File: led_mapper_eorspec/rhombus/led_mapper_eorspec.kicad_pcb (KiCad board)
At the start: 4 copper layers, 116 x 67 mm, 513 parts, among them J1 Conn_02x12_Top_Bottom

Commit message: sync PCB changes
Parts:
- moved J1 151.1 mm to (103.6, 41.4)
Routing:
- net /P6: track 91.7 -> 129.4 mm
- net /P1: track 96.8 -> 132.7 mm
- net /P2: track 94.7 -> 130.3 mm
- net /P3: track 94.7 -> 130.0 mm
- net /P4: track 94.7 -> 129.7 mm
- net /P5: track 94.7 -> 129.4 mm
- net /P7: track 94.7 -> 128.8 mm
- net /P8: track 96.8 -> 130.6 mm
- net /P23: track 100.0 -> 97.0 mm
- net /P19: track 114.7 -> 111.7 mm
- net /P16: track 114.7 -> 111.7 mm
- net /P13: track 114.7 -> 111.7 mm
- net /P10: track 114.7 -> 111.7 mm
- net /P22: track 100.0 -> 97.0 mm
- net /P20: track 100.0 -> 97.0 mm
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
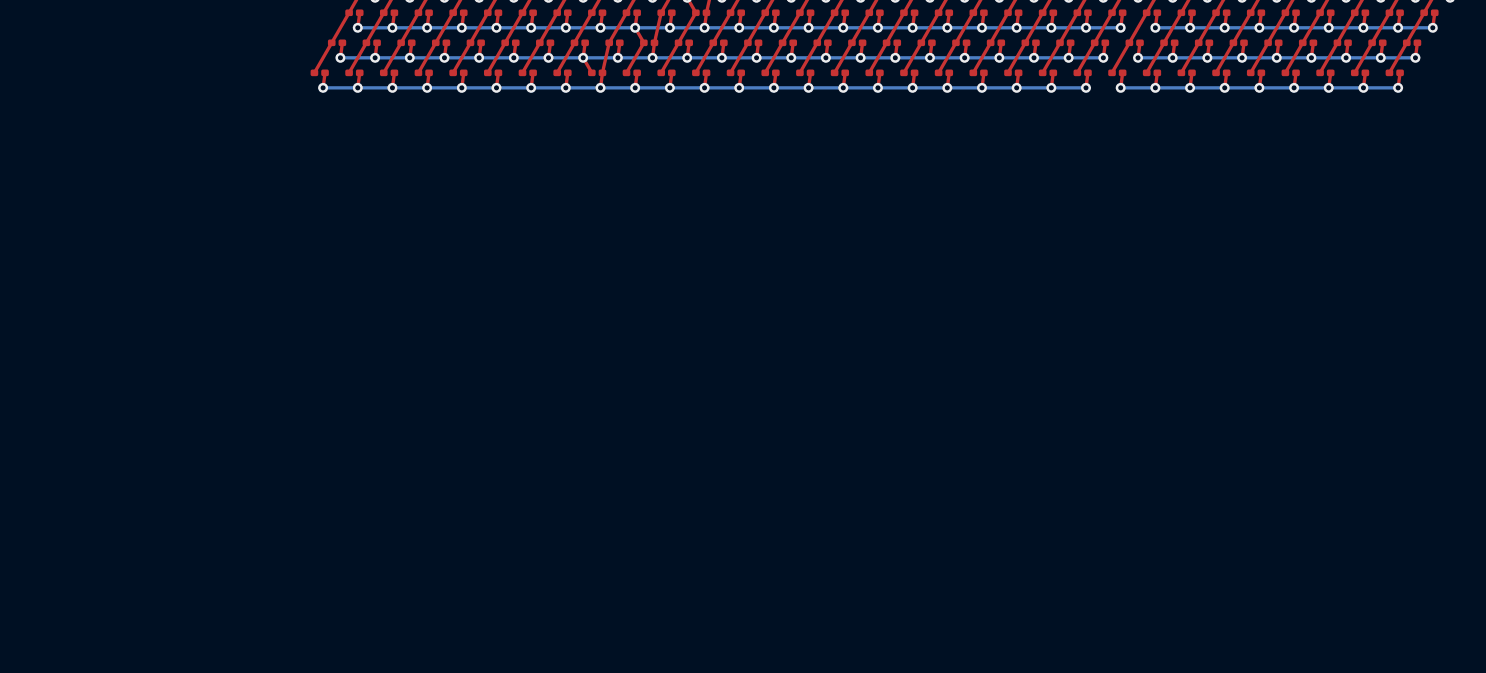
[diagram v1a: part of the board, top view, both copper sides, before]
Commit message: Add second network to PCB
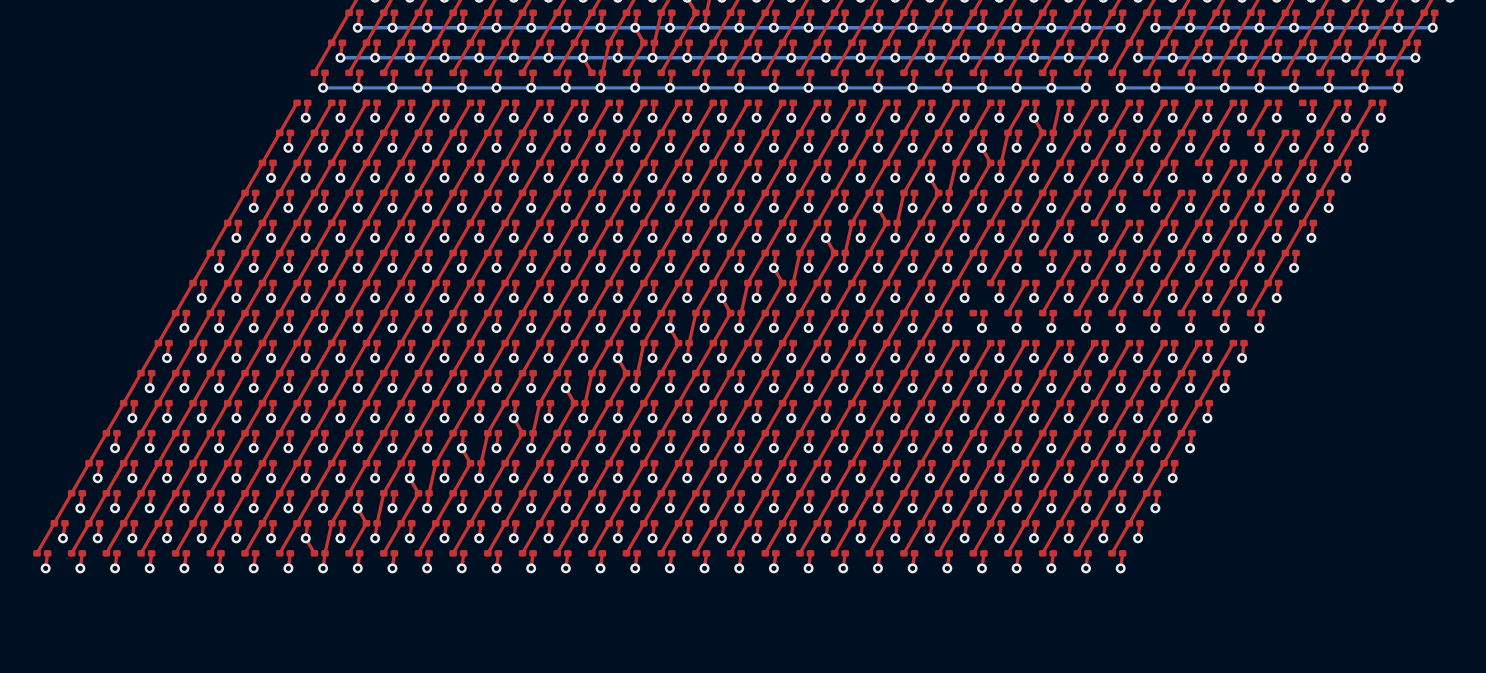
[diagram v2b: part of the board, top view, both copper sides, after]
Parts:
- added D1000: LED_45deg, LED_SMD:LED_0201_0603Metric, F.Cu at (13.9, 75.0)
- added D1001: LED_45deg, LED_SMD:LED_0201_0603Metric, F.Cu at (16.0, 75.0)
- added D1002: LED_45deg, LED_SMD:LED_0201_0603Metric, F.Cu at (18.1, 75.0)
- added D1003: LED_45deg, LED_SMD:LED_0201_0603Metric, F.Cu at (20.2, 75.0)
- added D1004: LED_45deg, LED_SMD:LED_0201_0603Metric, F.Cu at (22.3, 75.0)
- added D1005: LED_45deg, LED_SMD:LED_0201_0603Metric, F.Cu at (24.4, 75.0)
- added D1006: LED_45deg, LED_SMD:LED_0201_0603Metric, F.Cu at (26.4, 75.0)
- added D1007: LED_45deg, LED_SMD:LED_0201_0603Metric, F.Cu at (28.5, 75.0)
- added D1008: LED_45deg, LED_SMD:LED_0201_0603Metric, F.Cu at (30.6, 75.0)
- added D1009: LED_45deg, LED_SMD:LED_0201_0603Metric, F.Cu at (32.7, 75.0)
- added D1010: LED_45deg, LED_SMD:LED_0201_0603Metric, F.Cu at (34.8, 75.0)
- added D1011: LED_45deg, LED_SMD:LED_0201_0603Metric, F.Cu at (36.9, 75.0)
- added D1012: LED_45deg, LED_SMD:LED_0201_0603Metric, F.Cu at (39.0, 75.0)
- added D1013: LED_45deg, LED_SMD:LED_0201_0603Metric, F.Cu at (41.1, 75.0)
- added D1014: LED_45deg, LED_SMD:LED_0201_0603Metric, F.Cu at (43.2, 75.0)
- added D1015: LED_45deg, LED_SMD:LED_0201_0603Metric, F.Cu at (45.3, 75.0)
- added D1016: LED_45deg, LED_SMD:LED_0201_0603Metric, F.Cu at (47.4, 75.0)
- added D1017: LED_45deg, LED_SMD:LED_0201_0603Metric, F.Cu at (49.4, 75.0)
- added D1018: LED_45deg, LED_SMD:LED_0201_0603Metric, F.Cu at (51.5, 75.0)
- added D1019: LED_45deg, LED_SMD:LED_0201_0603Metric, F.Cu at (53.6, 75.0)
- added D1020: LED_45deg, LED_SMD:LED_0201_0603Metric, F.Cu at (55.7, 75.0)
- added D1021: LED_45deg, LED_SMD:LED_0201_0603Metric, F.Cu at (57.8, 75.0)
- added D1022: LED_45deg, LED_SMD:LED_0201_0603Metric, F.Cu at (59.9, 75.0)
- added D1023: LED_45deg, LED_SMD:LED_0201_0603Metric, F.Cu at (62.0, 75.0)
- added D1024: LED_45deg, LED_SMD:LED_0201_0603Metric, F.Cu at (64.1, 75.0)
- added D513: LED_45deg, LED_SMD:LED_0201_0603Metric, F.Cu at (15.0, 47.8)
- added D514: LED_45deg, LED_SMD:LED_0201_0603Metric, F.Cu at (17.0, 47.8)
- added D515: LED_45deg, LED_SMD:LED_0201_0603Metric, F.Cu at (19.1, 47.8)
- added D516: LED_45deg, LED_SMD:LED_0201_0603Metric, F.Cu at (21.2, 47.8)
- added D517: LED_45deg, LED_SMD:LED_0201_0603Metric, F.Cu at (23.3, 47.8)
- added D518: LED_45deg, LED_SMD:LED_0201_0603Metric, F.Cu at (25.4, 47.8)
- added D519: LED_45deg, LED_SMD:LED_0201_0603Metric, F.Cu at (27.5, 47.8)
- added D520: LED_45deg, LED_SMD:LED_0201_0603Metric, F.Cu at (29.6, 47.8)
- added D521: LED_45deg, LED_SMD:LED_0201_0603Metric, F.Cu at (31.7, 47.8)
- added D522: LED_45deg, LED_SMD:LED_0201_0603Metric, F.Cu at (33.8, 47.8)
- added D523: LED_45deg, LED_SMD:LED_0201_0603Metric, F.Cu at (35.9, 47.8)
- added D524: LED_45deg, LED_SMD:LED_0201_0603Metric, F.Cu at (37.9, 47.8)
- added D525: LED_45deg, LED_SMD:LED_0201_0603Metric, F.Cu at (40.0, 47.8)
- added D526: LED_45deg, LED_SMD:LED_0201_0603Metric, F.Cu at (42.1, 47.8)
- added D527: LED_45deg, LED_SMD:LED_0201_0603Metric, F.Cu at (44.2, 47.8)
- added D528: LED_45deg, LED_SMD:LED_0201_0603Metric, F.Cu at (46.3, 47.8)
- added D529: LED_45deg, LED_SMD:LED_0201_0603Metric, F.Cu at (48.4, 47.8)
- added D530: LED_45deg, LED_SMD:LED_0201_0603Metric, F.Cu at (50.5, 47.8)
- added D531: LED_45deg, LED_SMD:LED_0201_0603Metric, F.Cu at (52.6, 47.8)
- added D532: LED_45deg, LED_SMD:LED_0201_0603Metric, F.Cu at (54.7, 47.8)
- added D533: LED_45deg, LED_SMD:LED_0201_0603Metric, F.Cu at (56.8, 47.8)
- added D534: LED_45deg, LED_SMD:LED_0201_0603Metric, F.Cu at (58.8, 47.8)
- added D535: LED_45deg, LED_SMD:LED_0201_0603Metric, F.Cu at (60.9, 47.8)
- added D536: LED_45deg, LED_SMD:LED_0201_0603Metric, F.Cu at (63.0, 47.8)
- added D537: LED_45deg, LED_SMD:LED_0201_0603Metric, F.Cu at (65.1, 47.8)
- added D538: LED_45deg, LED_SMD:LED_0201_0603Metric, F.Cu at (67.2, 47.8)
- added D539: LED_45deg, LED_SMD:LED_0201_0603Metric, F.Cu at (69.3, 47.8)
- added D540: LED_45deg, LED_SMD:LED_0201_0603Metric, F.Cu at (71.4, 47.8)
- added D541: LED_45deg, LED_SMD:LED_0201_0603Metric, F.Cu at (73.5, 47.8)
- added D542: LED_45deg, LED_SMD:LED_0201_0603Metric, F.Cu at (75.6, 47.8)
- added D543: LED_45deg, LED_SMD:LED_0201_0603Metric, F.Cu at (77.7, 47.8)
- added D544: LED_45deg, LED_SMD:LED_0201_0603Metric, F.Cu at (79.7, 47.8)
- added D545: LED_45deg, LED_SMD:LED_0201_0603Metric, F.Cu at (13.9, 49.6)
- added D546: LED_45deg, LED_SMD:LED_0201_0603Metric, F.Cu at (16.0, 49.6)
- added D547: LED_45deg, LED_SMD:LED_0201_0603Metric, F.Cu at (18.1, 49.6)
- added D548: LED_45deg, LED_SMD:LED_0201_0603Metric, F.Cu at (20.2, 49.6)
- added D549: LED_45deg, LED_SMD:LED_0201_0603Metric, F.Cu at (22.3, 49.6)
- added D550: LED_45deg, LED_SMD:LED_0201_0603Metric, F.Cu at (24.4, 49.6)
- added D551: LED_45deg, LED_SMD:LED_0201_0603Metric, F.Cu at (26.4, 49.6)
- added D552: LED_45deg, LED_SMD:LED_0201_0603Metric, F.Cu at (28.5, 49.6)
- added D553: LED_45deg, LED_SMD:LED_0201_0603Metric, F.Cu at (30.6, 49.6)
- added D554: LED_45deg, LED_SMD:LED_0201_0603Metric, F.Cu at (32.7, 49.6)
- added D555: LED_45deg, LED_SMD:LED_0201_0603Metric, F.Cu at (34.8, 49.6)
- added D556: LED_45deg, LED_SMD:LED_0201_0603Metric, F.Cu at (36.9, 49.6)
- added D557: LED_45deg, LED_SMD:LED_0201_0603Metric, F.Cu at (39.0, 49.6)
- added D558: LED_45deg, LED_SMD:LED_0201_0603Metric, F.Cu at (41.1, 49.6)
- added D559: LED_45deg, LED_SMD:LED_0201_0603Metric, F.Cu at (43.2, 49.6)
- added D560: LED_45deg, LED_SMD:LED_0201_0603Metric, F.Cu at (45.3, 49.6)
- added D561: LED_45deg, LED_SMD:LED_0201_0603Metric, F.Cu at (47.4, 49.6)
- added D562: LED_45deg, LED_SMD:LED_0201_0603Metric, F.Cu at (49.4, 49.6)
- added D563: LED_45deg, LED_SMD:LED_0201_0603Metric, F.Cu at (51.5, 49.6)
- added D564: LED_45deg, LED_SMD:LED_0201_0603Metric, F.Cu at (53.6, 49.6)
- added D565: LED_45deg, LED_SMD:LED_0201_0603Metric, F.Cu at (55.7, 49.6)
- added D566: LED_45deg, LED_SMD:LED_0201_0603Metric, F.Cu at (57.8, 49.6)
- added D567: LED_45deg, LED_SMD:LED_0201_0603Metric, F.Cu at (59.9, 49.6)
- added D568: LED_45deg, LED_SMD:LED_0201_0603Metric, F.Cu at (62.0, 49.6)
- added D569: LED_45deg, LED_SMD:LED_0201_0603Metric, F.Cu at (64.1, 49.6)
- added D570: LED_45deg, LED_SMD:LED_0201_0603Metric, F.Cu at (66.2, 49.6)
- added D571: LED_45deg, LED_SMD:LED_0201_0603Metric, F.Cu at (68.2, 49.6)
- added D572: LED_45deg, LED_SMD:LED_0201_0603Metric, F.Cu at (70.3, 49.6)
- added D573: LED_45deg, LED_SMD:LED_0201_0603Metric, F.Cu at (72.4, 49.6)
- added D574: LED_45deg, LED_SMD:LED_0201_0603Metric, F.Cu at (74.5, 49.6)
- added D575: LED_45deg, LED_SMD:LED_0201_0603Metric, F.Cu at (76.6, 49.6)
- added D576: LED_45deg, LED_SMD:LED_0201_0603Metric, F.Cu at (78.7, 49.6)
- added D577: LED_45deg, LED_SMD:LED_0201_0603Metric, F.Cu at (12.9, 51.4)
- added D578: LED_45deg, LED_SMD:LED_0201_0603Metric, F.Cu at (15.0, 51.4)
- added D579: LED_45deg, LED_SMD:LED_0201_0603Metric, F.Cu at (17.0, 51.4)
- added D580: LED_45deg, LED_SMD:LED_0201_0603Metric, F.Cu at (19.1, 51.4)
- added D581: LED_45deg, LED_SMD:LED_0201_0603Metric, F.Cu at (21.2, 51.4)
- added D582: LED_45deg, LED_SMD:LED_0201_0603Metric, F.Cu at (23.3, 51.4)
- added D583: LED_45deg, LED_SMD:LED_0201_0603Metric, F.Cu at (25.4, 51.4)
- added D584: LED_45deg, LED_SMD:LED_0201_0603Metric, F.Cu at (27.5, 51.4)
- added D585: LED_45deg, LED_SMD:LED_0201_0603Metric, F.Cu at (29.6, 51.4)
- added D586: LED_45deg, LED_SMD:LED_0201_0603Metric, F.Cu at (31.7, 51.4)
- added D587: LED_45deg, LED_SMD:LED_0201_0603Metric, F.Cu at (33.8, 51.4)
- added D588: LED_45deg, LED_SMD:LED_0201_0603Metric, F.Cu at (35.9, 51.4)
- added D589: LED_45deg, LED_SMD:LED_0201_0603Metric, F.Cu at (37.9, 51.4)
- added D590: LED_45deg, LED_SMD:LED_0201_0603Metric, F.Cu at (40.0, 51.4)
- added D591: LED_45deg, LED_SMD:LED_0201_0603Metric, F.Cu at (42.1, 51.4)
- added D592: LED_45deg, LED_SMD:LED_0201_0603Metric, F.Cu at (44.2, 51.4)
- added D593: LED_45deg, LED_SMD:LED_0201_0603Metric, F.Cu at (46.3, 51.4)
- added D594: LED_45deg, LED_SMD:LED_0201_0603Metric, F.Cu at (48.4, 51.4)
- added D595: LED_45deg, LED_SMD:LED_0201_0603Metric, F.Cu at (50.5, 51.4)
- added D596: LED_45deg, LED_SMD:LED_0201_0603Metric, F.Cu at (52.6, 51.4)
- added D597: LED_45deg, LED_SMD:LED_0201_0603Metric, F.Cu at (54.7, 51.4)
- added D598: LED_45deg, LED_SMD:LED_0201_0603Metric, F.Cu at (56.8, 51.4)
- added D599: LED_45deg, LED_SMD:LED_0201_0603Metric, F.Cu at (58.8, 51.4)
- added D600: LED_45deg, LED_SMD:LED_0201_0603Metric, F.Cu at (60.9, 51.4)
- added D601: LED_45deg, LED_SMD:LED_0201_0603Metric, F.Cu at (63.0, 51.4)
- added D602: LED_45deg, LED_SMD:LED_0201_0603Metric, F.Cu at (65.1, 51.4)
- added D603: LED_45deg, LED_SMD:LED_0201_0603Metric, F.Cu at (67.2, 51.4)
- added D604: LED_45deg, LED_SMD:LED_0201_0603Metric, F.Cu at (69.3, 51.4)
- added D605: LED_45deg, LED_SMD:LED_0201_0603Metric, F.Cu at (71.4, 51.4)
- added D606: LED_45deg, LED_SMD:LED_0201_0603Metric, F.Cu at (73.5, 51.4)
- added D607: LED_45deg, LED_SMD:LED_0201_0603Metric, F.Cu at (75.6, 51.4)
- added D608: LED_45deg, LED_SMD:LED_0201_0603Metric, F.Cu at (77.7, 51.4)
- added D609: LED_45deg, LED_SMD:LED_0201_0603Metric, F.Cu at (11.8, 53.2)
- added D610: LED_45deg, LED_SMD:LED_0201_0603Metric, F.Cu at (13.9, 53.2)
- added D611: LED_45deg, LED_SMD:LED_0201_0603Metric, F.Cu at (16.0, 53.2)
- added D612: LED_45deg, LED_SMD:LED_0201_0603Metric, F.Cu at (18.1, 53.2)
- added D613: LED_45deg, LED_SMD:LED_0201_0603Metric, F.Cu at (20.2, 53.2)
- added D614: LED_45deg, LED_SMD:LED_0201_0603Metric, F.Cu at (22.3, 53.2)
- added D615: LED_45deg, LED_SMD:LED_0201_0603Metric, F.Cu at (24.4, 53.2)
- added D616: LED_45deg, LED_SMD:LED_0201_0603Metric, F.Cu at (26.4, 53.2)
- added D617: LED_45deg, LED_SMD:LED_0201_0603Metric, F.Cu at (28.5, 53.2)
- added D618: LED_45deg, LED_SMD:LED_0201_0603Metric, F.Cu at (30.6, 53.2)
- added D619: LED_45deg, LED_SMD:LED_0201_0603Metric, F.Cu at (32.7, 53.2)
- added D620: LED_45deg, LED_SMD:LED_0201_0603Metric, F.Cu at (34.8, 53.2)
- added D621: LED_45deg, LED_SMD:LED_0201_0603Metric, F.Cu at (36.9, 53.2)
- added D622: LED_45deg, LED_SMD:LED_0201_0603Metric, F.Cu at (39.0, 53.2)
- added D623: LED_45deg, LED_SMD:LED_0201_0603Metric, F.Cu at (41.1, 53.2)
- added D624: LED_45deg, LED_SMD:LED_0201_0603Metric, F.Cu at (43.2, 53.2)
- added D625: LED_45deg, LED_SMD:LED_0201_0603Metric, F.Cu at (45.3, 53.2)
- added D626: LED_45deg, LED_SMD:LED_0201_0603Metric, F.Cu at (47.4, 53.2)
- added D627: LED_45deg, LED_SMD:LED_0201_0603Metric, F.Cu at (49.4, 53.2)
- added D628: LED_45deg, LED_SMD:LED_0201_0603Metric, F.Cu at (51.5, 53.2)
- added D629: LED_45deg, LED_SMD:LED_0201_0603Metric, F.Cu at (53.6, 53.2)
- added D630: LED_45deg, LED_SMD:LED_0201_0603Metric, F.Cu at (55.7, 53.2)
- added D631: LED_45deg, LED_SMD:LED_0201_0603Metric, F.Cu at (57.8, 53.2)
- added D632: LED_45deg, LED_SMD:LED_0201_0603Metric, F.Cu at (59.9, 53.2)
- added D633: LED_45deg, LED_SMD:LED_0201_0603Metric, F.Cu at (62.0, 53.2)
- added D634: LED_45deg, LED_SMD:LED_0201_0603Metric, F.Cu at (64.1, 53.2)
- added D635: LED_45deg, LED_SMD:LED_0201_0603Metric, F.Cu at (66.2, 53.2)
- added D636: LED_45deg, LED_SMD:LED_0201_0603Metric, F.Cu at (68.2, 53.2)
- added D637: LED_45deg, LED_SMD:LED_0201_0603Metric, F.Cu at (70.3, 53.2)
- added D638: LED_45deg, LED_SMD:LED_0201_0603Metric, F.Cu at (72.4, 53.2)
- added D639: LED_45deg, LED_SMD:LED_0201_0603Metric, F.Cu at (74.5, 53.2)
- added D640: LED_45deg, LED_SMD:LED_0201_0603Metric, F.Cu at (76.6, 53.2)
- added D641: LED_45deg, LED_SMD:LED_0201_0603Metric, F.Cu at (10.8, 55.0)
- added D642: LED_45deg, LED_SMD:LED_0201_0603Metric, F.Cu at (12.9, 55.0)
- added D643: LED_45deg, LED_SMD:LED_0201_0603Metric, F.Cu at (15.0, 55.0)
- added D644: LED_45deg, LED_SMD:LED_0201_0603Metric, F.Cu at (17.0, 55.0)
- added D645: LED_45deg, LED_SMD:LED_0201_0603Metric, F.Cu at (19.1, 55.0)
- added D646: LED_45deg, LED_SMD:LED_0201_0603Metric, F.Cu at (21.2, 55.0)
- added D647: LED_45deg, LED_SMD:LED_0201_0603Metric, F.Cu at (23.3, 55.0)
- added D648: LED_45deg, LED_SMD:LED_0201_0603Metric, F.Cu at (25.4, 55.0)
- added D649: LED_45deg, LED_SMD:LED_0201_0603Metric, F.Cu at (27.5, 55.0)
- added D650: LED_45deg, LED_SMD:LED_0201_0603Metric, F.Cu at (29.6, 55.0)
- added D651: LED_45deg, LED_SMD:LED_0201_0603Metric, F.Cu at (31.7, 55.0)
- added D652: LED_45deg, LED_SMD:LED_0201_0603Metric, F.Cu at (33.8, 55.0)
- added D653: LED_45deg, LED_SMD:LED_0201_0603Metric, F.Cu at (35.9, 55.0)
- added D654: LED_45deg, LED_SMD:LED_0201_0603Metric, F.Cu at (37.9, 55.0)
- added D655: LED_45deg, LED_SMD:LED_0201_0603Metric, F.Cu at (40.0, 55.0)
- added D656: LED_45deg, LED_SMD:LED_0201_0603Metric, F.Cu at (42.1, 55.0)
- added D657: LED_45deg, LED_SMD:LED_0201_0603Metric, F.Cu at (44.2, 55.0)
- added D658: LED_45deg, LED_SMD:LED_0201_0603Metric, F.Cu at (46.3, 55.0)
- added D659: LED_45deg, LED_SMD:LED_0201_0603Metric, F.Cu at (48.4, 55.0)
- added D660: LED_45deg, LED_SMD:LED_0201_0603Metric, F.Cu at (50.5, 55.0)
- added D661: LED_45deg, LED_SMD:LED_0201_0603Metric, F.Cu at (52.6, 55.0)
- added D662: LED_45deg, LED_SMD:LED_0201_0603Metric, F.Cu at (54.7, 55.0)
- added D663: LED_45deg, LED_SMD:LED_0201_0603Metric, F.Cu at (56.8, 55.0)
- added D664: LED_45deg, LED_SMD:LED_0201_0603Metric, F.Cu at (58.8, 55.0)
- added D665: LED_45deg, LED_SMD:LED_0201_0603Metric, F.Cu at (60.9, 55.0)
- added D666: LED_45deg, LED_SMD:LED_0201_0603Metric, F.Cu at (63.0, 55.0)
- added D667: LED_45deg, LED_SMD:LED_0201_0603Metric, F.Cu at (65.1, 55.0)
- added D668: LED_45deg, LED_SMD:LED_0201_0603Metric, F.Cu at (67.2, 55.0)
- added D669: LED_45deg, LED_SMD:LED_0201_0603Metric, F.Cu at (69.3, 55.0)
- added D670: LED_45deg, LED_SMD:LED_0201_0603Metric, F.Cu at (71.4, 55.0)
- added D671: LED_45deg, LED_SMD:LED_0201_0603Metric, F.Cu at (73.5, 55.0)
- added D672: LED_45deg, LED_SMD:LED_0201_0603Metric, F.Cu at (75.6, 55.0)
- added D673: LED_45deg, LED_SMD:LED_0201_0603Metric, F.Cu at (9.73, 56.9)
- added D674: LED_45deg, LED_SMD:LED_0201_0603Metric, F.Cu at (11.8, 56.9)
- added D675: LED_45deg, LED_SMD:LED_0201_0603Metric, F.Cu at (13.9, 56.9)
- added D676: LED_45deg, LED_SMD:LED_0201_0603Metric, F.Cu at (16.0, 56.9)
- added D677: LED_45deg, LED_SMD:LED_0201_0603Metric, F.Cu at (18.1, 56.9)
- added D678: LED_45deg, LED_SMD:LED_0201_0603Metric, F.Cu at (20.2, 56.9)
- added D679: LED_45deg, LED_SMD:LED_0201_0603Metric, F.Cu at (22.3, 56.9)
- added D680: LED_45deg, LED_SMD:LED_0201_0603Metric, F.Cu at (24.4, 56.9)
- added D681: LED_45deg, LED_SMD:LED_0201_0603Metric, F.Cu at (26.4, 56.9)
- added D682: LED_45deg, LED_SMD:LED_0201_0603Metric, F.Cu at (28.5, 56.9)
- added D683: LED_45deg, LED_SMD:LED_0201_0603Metric, F.Cu at (30.6, 56.9)
- added D684: LED_45deg, LED_SMD:LED_0201_0603Metric, F.Cu at (32.7, 56.9)
- added D685: LED_45deg, LED_SMD:LED_0201_0603Metric, F.Cu at (34.8, 56.9)
- added D686: LED_45deg, LED_SMD:LED_0201_0603Metric, F.Cu at (36.9, 56.9)
- added D687: LED_45deg, LED_SMD:LED_0201_0603Metric, F.Cu at (39.0, 56.9)
- added D688: LED_45deg, LED_SMD:LED_0201_0603Metric, F.Cu at (41.1, 56.9)
- added D689: LED_45deg, LED_SMD:LED_0201_0603Metric, F.Cu at (43.2, 56.9)
- added D690: LED_45deg, LED_SMD:LED_0201_0603Metric, F.Cu at (45.3, 56.9)
- added D691: LED_45deg, LED_SMD:LED_0201_0603Metric, F.Cu at (47.4, 56.9)
- added D692: LED_45deg, LED_SMD:LED_0201_0603Metric, F.Cu at (49.4, 56.9)
- added D693: LED_45deg, LED_SMD:LED_0201_0603Metric, F.Cu at (51.5, 56.9)
- added D694: LED_45deg, LED_SMD:LED_0201_0603Metric, F.Cu at (53.6, 56.9)
- added D695: LED_45deg, LED_SMD:LED_0201_0603Metric, F.Cu at (55.7, 56.9)
- added D696: LED_45deg, LED_SMD:LED_0201_0603Metric, F.Cu at (57.8, 56.9)
- added D697: LED_45deg, LED_SMD:LED_0201_0603Metric, F.Cu at (59.9, 56.9)
- added D698: LED_45deg, LED_SMD:LED_0201_0603Metric, F.Cu at (62.0, 56.9)
- added D699: LED_45deg, LED_SMD:LED_0201_0603Metric, F.Cu at (64.1, 56.9)
- added D700: LED_45deg, LED_SMD:LED_0201_0603Metric, F.Cu at (66.2, 56.9)
- added D701: LED_45deg, LED_SMD:LED_0201_0603Metric, F.Cu at (68.2, 56.9)
- added D702: LED_45deg, LED_SMD:LED_0201_0603Metric, F.Cu at (70.3, 56.9)
- added D703: LED_45deg, LED_SMD:LED_0201_0603Metric, F.Cu at (72.4, 56.9)
- added D704: LED_45deg, LED_SMD:LED_0201_0603Metric, F.Cu at (74.5, 56.9)
- added D705: LED_45deg, LED_SMD:LED_0201_0603Metric, F.Cu at (8.69, 58.7)
- added D706: LED_45deg, LED_SMD:LED_0201_0603Metric, F.Cu at (10.8, 58.7)
- added D707: LED_45deg, LED_SMD:LED_0201_0603Metric, F.Cu at (12.9, 58.7)
- added D708: LED_45deg, LED_SMD:LED_0201_0603Metric, F.Cu at (15.0, 58.7)
- added D709: LED_45deg, LED_SMD:LED_0201_0603Metric, F.Cu at (17.0, 58.7)
- added D710: LED_45deg, LED_SMD:LED_0201_0603Metric, F.Cu at (19.1, 58.7)
- added D711: LED_45deg, LED_SMD:LED_0201_0603Metric, F.Cu at (21.2, 58.7)
- added D712: LED_45deg, LED_SMD:LED_0201_0603Metric, F.Cu at (23.3, 58.7)
- added D713: LED_45deg, LED_SMD:LED_0201_0603Metric, F.Cu at (25.4, 58.7)
- added D714: LED_45deg, LED_SMD:LED_0201_0603Metric, F.Cu at (27.5, 58.7)
- added D715: LED_45deg, LED_SMD:LED_0201_0603Metric, F.Cu at (29.6, 58.7)
- added D716: LED_45deg, LED_SMD:LED_0201_0603Metric, F.Cu at (31.7, 58.7)
- added D717: LED_45deg, LED_SMD:LED_0201_0603Metric, F.Cu at (33.8, 58.7)
- added D718: LED_45deg, LED_SMD:LED_0201_0603Metric, F.Cu at (35.9, 58.7)
- added D719: LED_45deg, LED_SMD:LED_0201_0603Metric, F.Cu at (37.9, 58.7)
- added D720: LED_45deg, LED_SMD:LED_0201_0603Metric, F.Cu at (40.0, 58.7)
- added D721: LED_45deg, LED_SMD:LED_0201_0603Metric, F.Cu at (42.1, 58.7)
- added D722: LED_45deg, LED_SMD:LED_0201_0603Metric, F.Cu at (44.2, 58.7)
- added D723: LED_45deg, LED_SMD:LED_0201_0603Metric, F.Cu at (46.3, 58.7)
- added D724: LED_45deg, LED_SMD:LED_0201_0603Metric, F.Cu at (48.4, 58.7)
- added D725: LED_45deg, LED_SMD:LED_0201_0603Metric, F.Cu at (50.5, 58.7)
- added D726: LED_45deg, LED_SMD:LED_0201_0603Metric, F.Cu at (52.6, 58.7)
- added D727: LED_45deg, LED_SMD:LED_0201_0603Metric, F.Cu at (54.7, 58.7)
- added D728: LED_45deg, LED_SMD:LED_0201_0603Metric, F.Cu at (56.8, 58.7)
- added D729: LED_45deg, LED_SMD:LED_0201_0603Metric, F.Cu at (58.8, 58.7)
- added D730: LED_45deg, LED_SMD:LED_0201_0603Metric, F.Cu at (60.9, 58.7)
- added D731: LED_45deg, LED_SMD:LED_0201_0603Metric, F.Cu at (63.0, 58.7)
- added D732: LED_45deg, LED_SMD:LED_0201_0603Metric, F.Cu at (65.1, 58.7)
- added D733: LED_45deg, LED_SMD:LED_0201_0603Metric, F.Cu at (67.2, 58.7)
- added D734: LED_45deg, LED_SMD:LED_0201_0603Metric, F.Cu at (69.3, 58.7)
- added D735: LED_45deg, LED_SMD:LED_0201_0603Metric, F.Cu at (71.4, 58.7)
- added D736: LED_45deg, LED_SMD:LED_0201_0603Metric, F.Cu at (73.5, 58.7)
- added D737: LED_45deg, LED_SMD:LED_0201_0603Metric, F.Cu at (7.64, 60.5)
- added D738: LED_45deg, LED_SMD:LED_0201_0603Metric, F.Cu at (9.73, 60.5)
- added D739: LED_45deg, LED_SMD:LED_0201_0603Metric, F.Cu at (11.8, 60.5)
- added D740: LED_45deg, LED_SMD:LED_0201_0603Metric, F.Cu at (13.9, 60.5)
- added D741: LED_45deg, LED_SMD:LED_0201_0603Metric, F.Cu at (16.0, 60.5)
- added D742: LED_45deg, LED_SMD:LED_0201_0603Metric, F.Cu at (18.1, 60.5)
- added D743: LED_45deg, LED_SMD:LED_0201_0603Metric, F.Cu at (20.2, 60.5)
- added D744: LED_45deg, LED_SMD:LED_0201_0603Metric, F.Cu at (22.3, 60.5)
- added D745: LED_45deg, LED_SMD:LED_0201_0603Metric, F.Cu at (24.4, 60.5)
- added D746: LED_45deg, LED_SMD:LED_0201_0603Metric, F.Cu at (26.4, 60.5)
- added D747: LED_45deg, LED_SMD:LED_0201_0603Metric, F.Cu at (28.5, 60.5)
- added D748: LED_45deg, LED_SMD:LED_0201_0603Metric, F.Cu at (30.6, 60.5)
- added D749: LED_45deg, LED_SMD:LED_0201_0603Metric, F.Cu at (32.7, 60.5)
- added D750: LED_45deg, LED_SMD:LED_0201_0603Metric, F.Cu at (34.8, 60.5)
- added D751: LED_45deg, LED_SMD:LED_0201_0603Metric, F.Cu at (36.9, 60.5)
- added D752: LED_45deg, LED_SMD:LED_0201_0603Metric, F.Cu at (39.0, 60.5)
- added D753: LED_45deg, LED_SMD:LED_0201_0603Metric, F.Cu at (41.1, 60.5)
- added D754: LED_45deg, LED_SMD:LED_0201_0603Metric, F.Cu at (43.2, 60.5)
- added D755: LED_45deg, LED_SMD:LED_0201_0603Metric, F.Cu at (45.3, 60.5)
- added D756: LED_45deg, LED_SMD:LED_0201_0603Metric, F.Cu at (47.4, 60.5)
- added D757: LED_45deg, LED_SMD:LED_0201_0603Metric, F.Cu at (49.4, 60.5)
- added D758: LED_45deg, LED_SMD:LED_0201_0603Metric, F.Cu at (51.5, 60.5)
- added D759: LED_45deg, LED_SMD:LED_0201_0603Metric, F.Cu at (53.6, 60.5)
- added D760: LED_45deg, LED_SMD:LED_0201_0603Metric, F.Cu at (55.7, 60.5)
- added D761: LED_45deg, LED_SMD:LED_0201_0603Metric, F.Cu at (57.8, 60.5)
- added D762: LED_45deg, LED_SMD:LED_0201_0603Metric, F.Cu at (59.9, 60.5)
- added D763: LED_45deg, LED_SMD:LED_0201_0603Metric, F.Cu at (62.0, 60.5)
- added D764: LED_45deg, LED_SMD:LED_0201_0603Metric, F.Cu at (64.1, 60.5)
- added D765: LED_45deg, LED_SMD:LED_0201_0603Metric, F.Cu at (66.2, 60.5)
- added D766: LED_45deg, LED_SMD:LED_0201_0603Metric, F.Cu at (68.2, 60.5)
- added D767: LED_45deg, LED_SMD:LED_0201_0603Metric, F.Cu at (70.3, 60.5)
- added D768: LED_45deg, LED_SMD:LED_0201_0603Metric, F.Cu at (72.4, 60.5)
- added D769: LED_45deg, LED_SMD:LED_0201_0603Metric, F.Cu at (6.59, 62.3)
- added D770: LED_45deg, LED_SMD:LED_0201_0603Metric, F.Cu at (8.69, 62.3)
- added D771: LED_45deg, LED_SMD:LED_0201_0603Metric, F.Cu at (10.8, 62.3)
- added D772: LED_45deg, LED_SMD:LED_0201_0603Metric, F.Cu at (12.9, 62.3)
- added D773: LED_45deg, LED_SMD:LED_0201_0603Metric, F.Cu at (15.0, 62.3)
- added D774: LED_45deg, LED_SMD:LED_0201_0603Metric, F.Cu at (17.0, 62.3)
- added D775: LED_45deg, LED_SMD:LED_0201_0603Metric, F.Cu at (19.1, 62.3)
- added D776: LED_45deg, LED_SMD:LED_0201_0603Metric, F.Cu at (21.2, 62.3)
- added D777: LED_45deg, LED_SMD:LED_0201_0603Metric, F.Cu at (23.3, 62.3)
- added D778: LED_45deg, LED_SMD:LED_0201_0603Metric, F.Cu at (25.4, 62.3)
- added D779: LED_45deg, LED_SMD:LED_0201_0603Metric, F.Cu at (27.5, 62.3)
- added D780: LED_45deg, LED_SMD:LED_0201_0603Metric, F.Cu at (29.6, 62.3)
- added D781: LED_45deg, LED_SMD:LED_0201_0603Metric, F.Cu at (31.7, 62.3)
- added D782: LED_45deg, LED_SMD:LED_0201_0603Metric, F.Cu at (33.8, 62.3)
- added D783: LED_45deg, LED_SMD:LED_0201_0603Metric, F.Cu at (35.9, 62.3)
- added D784: LED_45deg, LED_SMD:LED_0201_0603Metric, F.Cu at (37.9, 62.3)
- added D785: LED_45deg, LED_SMD:LED_0201_0603Metric, F.Cu at (40.0, 62.3)
- added D786: LED_45deg, LED_SMD:LED_0201_0603Metric, F.Cu at (42.1, 62.3)
- added D787: LED_45deg, LED_SMD:LED_0201_0603Metric, F.Cu at (44.2, 62.3)
- added D788: LED_45deg, LED_SMD:LED_0201_0603Metric, F.Cu at (46.3, 62.3)
- added D789: LED_45deg, LED_SMD:LED_0201_0603Metric, F.Cu at (48.4, 62.3)
- added D790: LED_45deg, LED_SMD:LED_0201_0603Metric, F.Cu at (50.5, 62.3)
- added D791: LED_45deg, LED_SMD:LED_0201_0603Metric, F.Cu at (52.6, 62.3)
- added D792: LED_45deg, LED_SMD:LED_0201_0603Metric, F.Cu at (54.7, 62.3)
- added D793: LED_45deg, LED_SMD:LED_0201_0603Metric, F.Cu at (56.8, 62.3)
- added D794: LED_45deg, LED_SMD:LED_0201_0603Metric, F.Cu at (58.8, 62.3)
- added D795: LED_45deg, LED_SMD:LED_0201_0603Metric, F.Cu at (60.9, 62.3)
- added D796: LED_45deg, LED_SMD:LED_0201_0603Metric, F.Cu at (63.0, 62.3)
- added D797: LED_45deg, LED_SMD:LED_0201_0603Metric, F.Cu at (65.1, 62.3)
- added D798: LED_45deg, LED_SMD:LED_0201_0603Metric, F.Cu at (67.2, 62.3)
- added D799: LED_45deg, LED_SMD:LED_0201_0603Metric, F.Cu at (69.3, 62.3)
- added D800: LED_45deg, LED_SMD:LED_0201_0603Metric, F.Cu at (71.4, 62.3)
- added D801: LED_45deg, LED_SMD:LED_0201_0603Metric, F.Cu at (5.55, 64.1)
- added D802: LED_45deg, LED_SMD:LED_0201_0603Metric, F.Cu at (7.64, 64.1)
- added D803: LED_45deg, LED_SMD:LED_0201_0603Metric, F.Cu at (9.73, 64.1)
- added D804: LED_45deg, LED_SMD:LED_0201_0603Metric, F.Cu at (11.8, 64.1)
- added D805: LED_45deg, LED_SMD:LED_0201_0603Metric, F.Cu at (13.9, 64.1)
- added D806: LED_45deg, LED_SMD:LED_0201_0603Metric, F.Cu at (16.0, 64.1)
- added D807: LED_45deg, LED_SMD:LED_0201_0603Metric, F.Cu at (18.1, 64.1)
- added D808: LED_45deg, LED_SMD:LED_0201_0603Metric, F.Cu at (20.2, 64.1)
- added D809: LED_45deg, LED_SMD:LED_0201_0603Metric, F.Cu at (22.3, 64.1)
- added D810: LED_45deg, LED_SMD:LED_0201_0603Metric, F.Cu at (24.4, 64.1)
- added D811: LED_45deg, LED_SMD:LED_0201_0603Metric, F.Cu at (26.4, 64.1)
- added D812: LED_45deg, LED_SMD:LED_0201_0603Metric, F.Cu at (28.5, 64.1)
- added D813: LED_45deg, LED_SMD:LED_0201_0603Metric, F.Cu at (30.6, 64.1)
- added D814: LED_45deg, LED_SMD:LED_0201_0603Metric, F.Cu at (32.7, 64.1)
- added D815: LED_45deg, LED_SMD:LED_0201_0603Metric, F.Cu at (34.8, 64.1)
- added D816: LED_45deg, LED_SMD:LED_0201_0603Metric, F.Cu at (36.9, 64.1)
- added D817: LED_45deg, LED_SMD:LED_0201_0603Metric, F.Cu at (39.0, 64.1)
- added D818: LED_45deg, LED_SMD:LED_0201_0603Metric, F.Cu at (41.1, 64.1)
- added D819: LED_45deg, LED_SMD:LED_0201_0603Metric, F.Cu at (43.2, 64.1)
- added D820: LED_45deg, LED_SMD:LED_0201_0603Metric, F.Cu at (45.3, 64.1)
- added D821: LED_45deg, LED_SMD:LED_0201_0603Metric, F.Cu at (47.4, 64.1)
- added D822: LED_45deg, LED_SMD:LED_0201_0603Metric, F.Cu at (49.4, 64.1)
- added D823: LED_45deg, LED_SMD:LED_0201_0603Metric, F.Cu at (51.5, 64.1)
- added D824: LED_45deg, LED_SMD:LED_0201_0603Metric, F.Cu at (53.6, 64.1)
- added D825: LED_45deg, LED_SMD:LED_0201_0603Metric, F.Cu at (55.7, 64.1)
- added D826: LED_45deg, LED_SMD:LED_0201_0603Metric, F.Cu at (57.8, 64.1)
- added D827: LED_45deg, LED_SMD:LED_0201_0603Metric, F.Cu at (59.9, 64.1)
- added D828: LED_45deg, LED_SMD:LED_0201_0603Metric, F.Cu at (62.0, 64.1)
- added D829: LED_45deg, LED_SMD:LED_0201_0603Metric, F.Cu at (64.1, 64.1)
- added D830: LED_45deg, LED_SMD:LED_0201_0603Metric, F.Cu at (66.2, 64.1)
- added D831: LED_45deg, LED_SMD:LED_0201_0603Metric, F.Cu at (68.2, 64.1)
- added D832: LED_45deg, LED_SMD:LED_0201_0603Metric, F.Cu at (70.3, 64.1)
- added D833: LED_45deg, LED_SMD:LED_0201_0603Metric, F.Cu at (4.50, 65.9)
- added D834: LED_45deg, LED_SMD:LED_0201_0603Metric, F.Cu at (6.59, 65.9)
- added D835: LED_45deg, LED_SMD:LED_0201_0603Metric, F.Cu at (8.69, 65.9)
- added D836: LED_45deg, LED_SMD:LED_0201_0603Metric, F.Cu at (10.8, 65.9)
- added D837: LED_45deg, LED_SMD:LED_0201_0603Metric, F.Cu at (12.9, 65.9)
- added D838: LED_45deg, LED_SMD:LED_0201_0603Metric, F.Cu at (15.0, 65.9)
- added D839: LED_45deg, LED_SMD:LED_0201_0603Metric, F.Cu at (17.0, 65.9)
- added D840: LED_45deg, LED_SMD:LED_0201_0603Metric, F.Cu at (19.1, 65.9)
- added D841: LED_45deg, LED_SMD:LED_0201_0603Metric, F.Cu at (21.2, 65.9)
- added D842: LED_45deg, LED_SMD:LED_0201_0603Metric, F.Cu at (23.3, 65.9)
- added D843: LED_45deg, LED_SMD:LED_0201_0603Metric, F.Cu at (25.4, 65.9)
- added D844: LED_45deg, LED_SMD:LED_0201_0603Metric, F.Cu at (27.5, 65.9)
- added D845: LED_45deg, LED_SMD:LED_0201_0603Metric, F.Cu at (29.6, 65.9)
- added D846: LED_45deg, LED_SMD:LED_0201_0603Metric, F.Cu at (31.7, 65.9)
- added D847: LED_45deg, LED_SMD:LED_0201_0603Metric, F.Cu at (33.8, 65.9)
- added D848: LED_45deg, LED_SMD:LED_0201_0603Metric, F.Cu at (35.9, 65.9)
- added D849: LED_45deg, LED_SMD:LED_0201_0603Metric, F.Cu at (37.9, 65.9)
- added D850: LED_45deg, LED_SMD:LED_0201_0603Metric, F.Cu at (40.0, 65.9)
- added D851: LED_45deg, LED_SMD:LED_0201_0603Metric, F.Cu at (42.1, 65.9)
- added D852: LED_45deg, LED_SMD:LED_0201_0603Metric, F.Cu at (44.2, 65.9)
- added D853: LED_45deg, LED_SMD:LED_0201_0603Metric, F.Cu at (46.3, 65.9)
- added D854: LED_45deg, LED_SMD:LED_0201_0603Metric, F.Cu at (48.4, 65.9)
- added D855: LED_45deg, LED_SMD:LED_0201_0603Metric, F.Cu at (50.5, 65.9)
- added D856: LED_45deg, LED_SMD:LED_0201_0603Metric, F.Cu at (52.6, 65.9)
- added D857: LED_45deg, LED_SMD:LED_0201_0603Metric, F.Cu at (54.7, 65.9)
- added D858: LED_45deg, LED_SMD:LED_0201_0603Metric, F.Cu at (56.8, 65.9)
- added D859: LED_45deg, LED_SMD:LED_0201_0603Metric, F.Cu at (58.8, 65.9)
- added D860: LED_45deg, LED_SMD:LED_0201_0603Metric, F.Cu at (60.9, 65.9)
- added D861: LED_45deg, LED_SMD:LED_0201_0603Metric, F.Cu at (63.0, 65.9)
- added D862: LED_45deg, LED_SMD:LED_0201_0603Metric, F.Cu at (65.1, 65.9)
- added D863: LED_45deg, LED_SMD:LED_0201_0603Metric, F.Cu at (67.2, 65.9)
- added D864: LED_45deg, LED_SMD:LED_0201_0603Metric, F.Cu at (69.3, 65.9)
- added D865: LED_45deg, LED_SMD:LED_0201_0603Metric, F.Cu at (3.46, 67.7)
- added D866: LED_45deg, LED_SMD:LED_0201_0603Metric, F.Cu at (5.55, 67.7)
- added D867: LED_45deg, LED_SMD:LED_0201_0603Metric, F.Cu at (7.64, 67.7)
- added D868: LED_45deg, LED_SMD:LED_0201_0603Metric, F.Cu at (9.73, 67.7)
- added D869: LED_45deg, LED_SMD:LED_0201_0603Metric, F.Cu at (11.8, 67.7)
- added D870: LED_45deg, LED_SMD:LED_0201_0603Metric, F.Cu at (13.9, 67.7)
- added D871: LED_45deg, LED_SMD:LED_0201_0603Metric, F.Cu at (16.0, 67.7)
- added D872: LED_45deg, LED_SMD:LED_0201_0603Metric, F.Cu at (18.1, 67.7)
- added D873: LED_45deg, LED_SMD:LED_0201_0603Metric, F.Cu at (20.2, 67.7)
- added D874: LED_45deg, LED_SMD:LED_0201_0603Metric, F.Cu at (22.3, 67.7)
- added D875: LED_45deg, LED_SMD:LED_0201_0603Metric, F.Cu at (24.4, 67.7)
- added D876: LED_45deg, LED_SMD:LED_0201_0603Metric, F.Cu at (26.4, 67.7)
- added D877: LED_45deg, LED_SMD:LED_0201_0603Metric, F.Cu at (28.5, 67.7)
- added D878: LED_45deg, LED_SMD:LED_0201_0603Metric, F.Cu at (30.6, 67.7)
- added D879: LED_45deg, LED_SMD:LED_0201_0603Metric, F.Cu at (32.7, 67.7)
- added D880: LED_45deg, LED_SMD:LED_0201_0603Metric, F.Cu at (34.8, 67.7)
- added D881: LED_45deg, LED_SMD:LED_0201_0603Metric, F.Cu at (36.9, 67.7)
- added D882: LED_45deg, LED_SMD:LED_0201_0603Metric, F.Cu at (39.0, 67.7)
- added D883: LED_45deg, LED_SMD:LED_0201_0603Metric, F.Cu at (41.1, 67.7)
- added D884: LED_45deg, LED_SMD:LED_0201_0603Metric, F.Cu at (43.2, 67.7)
- added D885: LED_45deg, LED_SMD:LED_0201_0603Metric, F.Cu at (45.3, 67.7)
- added D886: LED_45deg, LED_SMD:LED_0201_0603Metric, F.Cu at (47.4, 67.7)
- added D887: LED_45deg, LED_SMD:LED_0201_0603Metric, F.Cu at (49.4, 67.7)
- added D888: LED_45deg, LED_SMD:LED_0201_0603Metric, F.Cu at (51.5, 67.7)
- added D889: LED_45deg, LED_SMD:LED_0201_0603Metric, F.Cu at (53.6, 67.7)
- added D890: LED_45deg, LED_SMD:LED_0201_0603Metric, F.Cu at (55.7, 67.7)
- added D891: LED_45deg, LED_SMD:LED_0201_0603Metric, F.Cu at (57.8, 67.7)
- added D892: LED_45deg, LED_SMD:LED_0201_0603Metric, F.Cu at (59.9, 67.7)
- added D893: LED_45deg, LED_SMD:LED_0201_0603Metric, F.Cu at (62.0, 67.7)
- added D894: LED_45deg, LED_SMD:LED_0201_0603Metric, F.Cu at (64.1, 67.7)
- added D895: LED_45deg, LED_SMD:LED_0201_0603Metric, F.Cu at (66.2, 67.7)
- added D896: LED_45deg, LED_SMD:LED_0201_0603Metric, F.Cu at (68.2, 67.7)
- added D897: LED_45deg, LED_SMD:LED_0201_0603Metric, F.Cu at (2.42, 69.5)
- added D898: LED_45deg, LED_SMD:LED_0201_0603Metric, F.Cu at (4.50, 69.5)
- added D899: LED_45deg, LED_SMD:LED_0201_0603Metric, F.Cu at (6.59, 69.5)
- added D900: LED_45deg, LED_SMD:LED_0201_0603Metric, F.Cu at (8.69, 69.5)
- added D901: LED_45deg, LED_SMD:LED_0201_0603Metric, F.Cu at (10.8, 69.5)
- added D902: LED_45deg, LED_SMD:LED_0201_0603Metric, F.Cu at (12.9, 69.5)
- added D903: LED_45deg, LED_SMD:LED_0201_0603Metric, F.Cu at (15.0, 69.5)
- added D904: LED_45deg, LED_SMD:LED_0201_0603Metric, F.Cu at (17.0, 69.5)
- added D905: LED_45deg, LED_SMD:LED_0201_0603Metric, F.Cu at (19.1, 69.5)
- added D906: LED_45deg, LED_SMD:LED_0201_0603Metric, F.Cu at (21.2, 69.5)
- added D907: LED_45deg, LED_SMD:LED_0201_0603Metric, F.Cu at (23.3, 69.5)
- added D908: LED_45deg, LED_SMD:LED_0201_0603Metric, F.Cu at (25.4, 69.5)
- added D909: LED_45deg, LED_SMD:LED_0201_0603Metric, F.Cu at (27.5, 69.5)
- added D910: LED_45deg, LED_SMD:LED_0201_0603Metric, F.Cu at (29.6, 69.5)
- added D911: LED_45deg, LED_SMD:LED_0201_0603Metric, F.Cu at (31.7, 69.5)
- added D912: LED_45deg, LED_SMD:LED_0201_0603Metric, F.Cu at (33.8, 69.5)
- added D913: LED_45deg, LED_SMD:LED_0201_0603Metric, F.Cu at (35.9, 69.5)
- added D914: LED_45deg, LED_SMD:LED_0201_0603Metric, F.Cu at (37.9, 69.5)
- added D915: LED_45deg, LED_SMD:LED_0201_0603Metric, F.Cu at (40.0, 69.5)
- added D916: LED_45deg, LED_SMD:LED_0201_0603Metric, F.Cu at (42.1, 69.5)
- added D917: LED_45deg, LED_SMD:LED_0201_0603Metric, F.Cu at (44.2, 69.5)
- added D918: LED_45deg, LED_SMD:LED_0201_0603Metric, F.Cu at (46.3, 69.5)
- added D919: LED_45deg, LED_SMD:LED_0201_0603Metric, F.Cu at (48.4, 69.5)
- added D920: LED_45deg, LED_SMD:LED_0201_0603Metric, F.Cu at (50.5, 69.5)
- added D921: LED_45deg, LED_SMD:LED_0201_0603Metric, F.Cu at (52.6, 69.5)
- added D922: LED_45deg, LED_SMD:LED_0201_0603Metric, F.Cu at (54.7, 69.5)
- added D923: LED_45deg, LED_SMD:LED_0201_0603Metric, F.Cu at (56.8, 69.5)
- added D924: LED_45deg, LED_SMD:LED_0201_0603Metric, F.Cu at (58.8, 69.5)
- added D925: LED_45deg, LED_SMD:LED_0201_0603Metric, F.Cu at (60.9, 69.5)
- added D926: LED_45deg, LED_SMD:LED_0201_0603Metric, F.Cu at (63.0, 69.5)
- added D927: LED_45deg, LED_SMD:LED_0201_0603Metric, F.Cu at (65.1, 69.5)
- added D928: LED_45deg, LED_SMD:LED_0201_0603Metric, F.Cu at (67.2, 69.5)
- added D929: LED_45deg, LED_SMD:LED_0201_0603Metric, F.Cu at (1.37, 71.3)
- added D930: LED_45deg, LED_SMD:LED_0201_0603Metric, F.Cu at (3.46, 71.3)
- added D931: LED_45deg, LED_SMD:LED_0201_0603Metric, F.Cu at (5.55, 71.3)
- added D932: LED_45deg, LED_SMD:LED_0201_0603Metric, F.Cu at (7.64, 71.3)
- added D933: LED_45deg, LED_SMD:LED_0201_0603Metric, F.Cu at (9.73, 71.3)
- added D934: LED_45deg, LED_SMD:LED_0201_0603Metric, F.Cu at (11.8, 71.3)
- added D935: LED_45deg, LED_SMD:LED_0201_0603Metric, F.Cu at (13.9, 71.3)
- added D936: LED_45deg, LED_SMD:LED_0201_0603Metric, F.Cu at (16.0, 71.3)
- added D937: LED_45deg, LED_SMD:LED_0201_0603Metric, F.Cu at (18.1, 71.3)
- added D938: LED_45deg, LED_SMD:LED_0201_0603Metric, F.Cu at (20.2, 71.3)
- added D939: LED_45deg, LED_SMD:LED_0201_0603Metric, F.Cu at (22.3, 71.3)
- added D940: LED_45deg, LED_SMD:LED_0201_0603Metric, F.Cu at (24.4, 71.3)
- added D941: LED_45deg, LED_SMD:LED_0201_0603Metric, F.Cu at (26.4, 71.3)
- added D942: LED_45deg, LED_SMD:LED_0201_0603Metric, F.Cu at (28.5, 71.3)
- added D943: LED_45deg, LED_SMD:LED_0201_0603Metric, F.Cu at (30.6, 71.3)
- added D944: LED_45deg, LED_SMD:LED_0201_0603Metric, F.Cu at (32.7, 71.3)
- added D945: LED_45deg, LED_SMD:LED_0201_0603Metric, F.Cu at (34.8, 71.3)
- added D946: LED_45deg, LED_SMD:LED_0201_0603Metric, F.Cu at (36.9, 71.3)
- added D947: LED_45deg, LED_SMD:LED_0201_0603Metric, F.Cu at (39.0, 71.3)
- added D948: LED_45deg, LED_SMD:LED_0201_0603Metric, F.Cu at (41.1, 71.3)
- added D949: LED_45deg, LED_SMD:LED_0201_0603Metric, F.Cu at (43.2, 71.3)
- added D950: LED_45deg, LED_SMD:LED_0201_0603Metric, F.Cu at (45.3, 71.3)
- added D951: LED_45deg, LED_SMD:LED_0201_0603Metric, F.Cu at (47.4, 71.3)
- added D952: LED_45deg, LED_SMD:LED_0201_0603Metric, F.Cu at (49.4, 71.3)
- added D953: LED_45deg, LED_SMD:LED_0201_0603Metric, F.Cu at (51.5, 71.3)
- added D954: LED_45deg, LED_SMD:LED_0201_0603Metric, F.Cu at (53.6, 71.3)
- added D955: LED_45deg, LED_SMD:LED_0201_0603Metric, F.Cu at (55.7, 71.3)
- added D956: LED_45deg, LED_SMD:LED_0201_0603Metric, F.Cu at (57.8, 71.3)
- added D957: LED_45deg, LED_SMD:LED_0201_0603Metric, F.Cu at (59.9, 71.3)
- added D958: LED_45deg, LED_SMD:LED_0201_0603Metric, F.Cu at (62.0, 71.3)
- added D959: LED_45deg, LED_SMD:LED_0201_0603Metric, F.Cu at (64.1, 71.3)
- added D960: LED_45deg, LED_SMD:LED_0201_0603Metric, F.Cu at (66.2, 71.3)
- added D961: LED_45deg, LED_SMD:LED_0201_0603Metric, F.Cu at (0.33, 73.1)
- added D962: LED_45deg, LED_SMD:LED_0201_0603Metric, F.Cu at (2.42, 73.1)
- added D963: LED_45deg, LED_SMD:LED_0201_0603Metric, F.Cu at (4.50, 73.1)
- added D964: LED_45deg, LED_SMD:LED_0201_0603Metric, F.Cu at (6.59, 73.1)
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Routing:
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
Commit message: Add track connections on front and back layer based on ratsnest
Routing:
- net /P11: track 177.4 -> 228.3 mm
- net /P20: track 148.1 -> 196.7 mm
- net /P21: track 148.1 -> 196.6 mm
- net /P17: track 177.4 -> 225.8 mm
- net /P15: track 178.1 -> 226.6 mm
- net /P14: track 177.4 -> 225.8 mm
- net /P23: track 148.1 -> 196.6 mm
- net /P22: track 148.1 -> 196.6 mm
- net /P19: track 177.4 -> 225.8 mm
- net /P16: track 177.4 -> 225.8 mm
- net /P18: track 177.4 -> 225.8 mm
- net /P13: track 177.4 -> 225.8 mm
- net /P12: track 177.4 -> 225.8 mm
- net /P10: track 177.4 -> 225.8 mm
- net /P24: track 148.6 -> 196.5 mm
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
